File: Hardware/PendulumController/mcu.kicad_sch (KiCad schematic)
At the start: 21 parts, among them J201 ICSP, SW201 RESET, SW202 START_SW, SW203 STOP/MODE_SW, U201 ATmega328P, Y201 16mHz

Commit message: Small layout improvements
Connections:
- net SCK: no longer D201.2 (A)
- net STAT_LED: now reaches U201.14 (PB2)
- net STAT_LED: now also D201.2 (A)
- no-connect marks 8 -> 7
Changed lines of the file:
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@@
   (no_connect (at 27.305 56.515))
   (no_connect (at 48.26 154.94))
-  (no_connect (at 57.785 53.975))
   (no_connect (at 57.785 109.855))
   (no_connect (at 48.26 157.48))
@@
   (no_connect (at 35.56 152.4))
   (no_connect (at 27.305 53.975))
+  (wire (pts (xy 57.785 53.975) (xy 79.375 53.975))
+    (stroke (width 0) (type default) (color 0 0 0 0))
+  )
   (wire (pts (xy 129.54 92.075) (xy 129.54 93.345))
     (stroke (width 0) (type default) (color 0 0 0 0))
@@
     (stroke (width 0) (type default) (color 0 0 0 0))
   )
-  (wire (pts (xy 92.71 60.325) (xy 97.79 60.325))
+  (wire (pts (xy 88.265 60.325) (xy 97.79 60.325))
     (stroke (width 0) (type default) (color 0 0 0 0))
   )
@@
     (effects (font (size 1.27 1.27)) (justify right bottom))
   )
-  (label "SCK" (at 92.71 60.325 0)
+  (label "STAT_LED" (at 88.265 60.325 0)
     (effects (font (size 1.27 1.27)) (justify left bottom))
   )
@@
     (effects (font (size 1.27 1.27)) (justify right bottom))
   )
+  (label "STAT_LED" (at 79.375 53.975 180)
+    (effects (font (size 1.27 1.27)) (justify right bottom))
+  )

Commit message: Add new connector
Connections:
- net TFT_DC: now reaches U201.11 (PD7)
- net TFT_A0 renamed SD_CS
- no-connect marks 7 -> 6

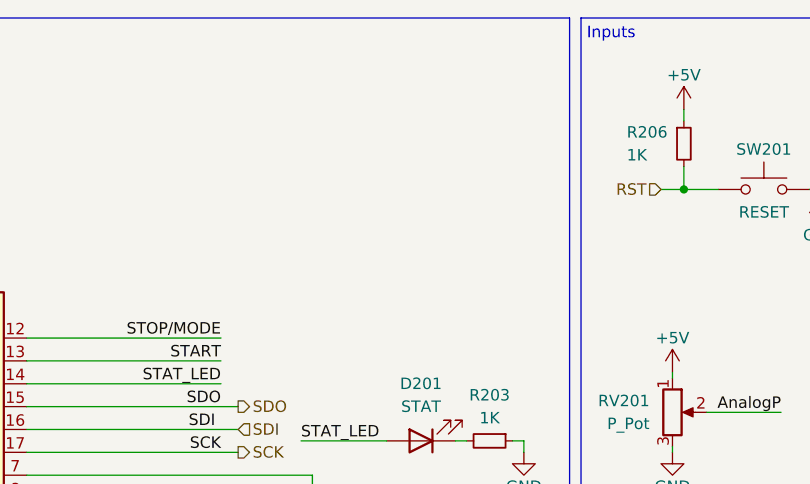
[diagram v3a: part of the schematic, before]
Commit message: Add limit siwtch
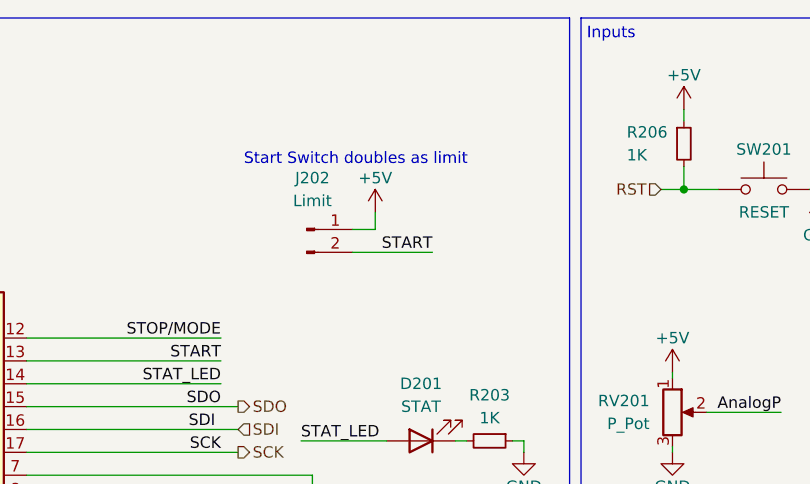
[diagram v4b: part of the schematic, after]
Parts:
- added J202: Limit, Connector_JST:JST_EH_B2B-EH-A_1x02_P2.50mm_Vertical, symbol Connector:Conn_01x02_Male
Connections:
- net +5V: now also J202.1 (Pin_1)
- net START: now also J202.2 (Pin_2)
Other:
- note added: "Start Switch doubles as limit"
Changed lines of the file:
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@@
   (no_connect (at 35.56 152.4))
   (no_connect (at 27.305 53.975))
+  (wire (pts (xy 102.87 39.37) (xy 93.98 39.37))
+    (stroke (width 0) (type default) (color 0 0 0 0))
+  )
   (wire (pts (xy 57.785 53.975) (xy 79.375 53.975))
     (stroke (width 0) (type default) (color 0 0 0 0))
@@
     (stroke (width 0) (type default) (color 0 0 0 0))
   )
+  (wire (pts (xy 96.52 36.83) (xy 93.98 36.83))
+    (stroke (width 0) (type default) (color 0 0 0 0))
+  )
   (wire (pts (xy 100.33 92.075) (xy 106.68 92.075))
     (stroke (width 0) (type default) (color 0 0 0 0))
@@
     (stroke (width 0) (type default) (color 0 0 0 0))
   )
+  (wire (pts (xy 96.52 34.925) (xy 96.52 36.83))
+    (stroke (width 0) (type default) (color 0 0 0 0))
+  )
   (wire (pts (xy 173.355 51.435) (xy 173.355 53.34))
     (stroke (width 0) (type default) (color 0 0 0 0))
@@
     (effects (font (size 1.27 1.27)) (justify left bottom))
   )
+  (text "Start Switch doubles as limit" (at 81.915 29.845 0)
+    (effects (font (size 1.27 1.27)) (justify left bottom))
+  )
   (text "MCU" (at 13.97 15.875 0)
     (effects (font (size 1.27 1.27)) (justify left bottom))
@@
   )
   (label "ICSP_RST" (at 87.63 88.9 180)
+    (effects (font (size 1.27 1.27)) (justify right bottom))
+  )
+  (label "START" (at 102.87 39.37 180)
     (effects (font (size 1.27 1.27)) (justify right bottom))
   )
@@
     )
     (property "Datasheet" "" (id 3) (at 187.96 41.91 0)
+      (effects (font (size 1.27 1.27)) hide)
+    )
+    (pin "1")
+  )
+  (symbol (lib_name "+5V_3") (lib_id "power:+5V") (at 96.52 34.925 0) (unit 1)
+    (in_bom yes) (on_board yes)
+    (property "Reference" "#PWR0146" (id 0) (at 96.52 38.735 0)
+      (effects (font (size 1.27 1.27)) hide)
+    )
+    (property "Value" "+5V" (id 1) (at 96.52 31.115 0))
+    (property "Footprint" "" (id 2) (at 96.52 34.925 0)
+      (effects (font (size 1.27 1.27)) hide)
+    )
+    (property "Datasheet" "" (id 3) (at 96.52 34.925 0)
       (effects (font (size 1.27 1.27)) hide)
     )
@@
     (pin "1")
   )
+  (symbol (lib_id "Connector:Conn_01x02_Male") (at 88.9 36.83 0) (unit 1)
+    (in_bom yes) (on_board yes) (fields_autoplaced)
+    (property "Reference" "J202" (id 0) (at 89.535 31.115 0))
+    (property "Value" "Limit" (id 1) (at 89.535 33.655 0))
+    (property "Footprint" "Connector_JST:JST_EH_B2B-EH-A_1x02_P2.50mm_Vertical" (id 2) (at 88.9 36.83 0)
+      (effects (font (size 1.27 1.27)) hide)
+    )
+    (property "Datasheet" "~" (id 3) (at 88.9 36.83 0)
+      (effects (font (size 1.27 1.27)) hide)
+    )
+    (pin "1")
+    (pin "2")
+  )
   (symbol (lib_id "Device:C_Small") (at 38.1 33.02 0) (unit 1)
